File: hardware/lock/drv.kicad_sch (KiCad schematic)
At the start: 9 parts, among them J3 SOLENOID 12V, Q1 AO3400A

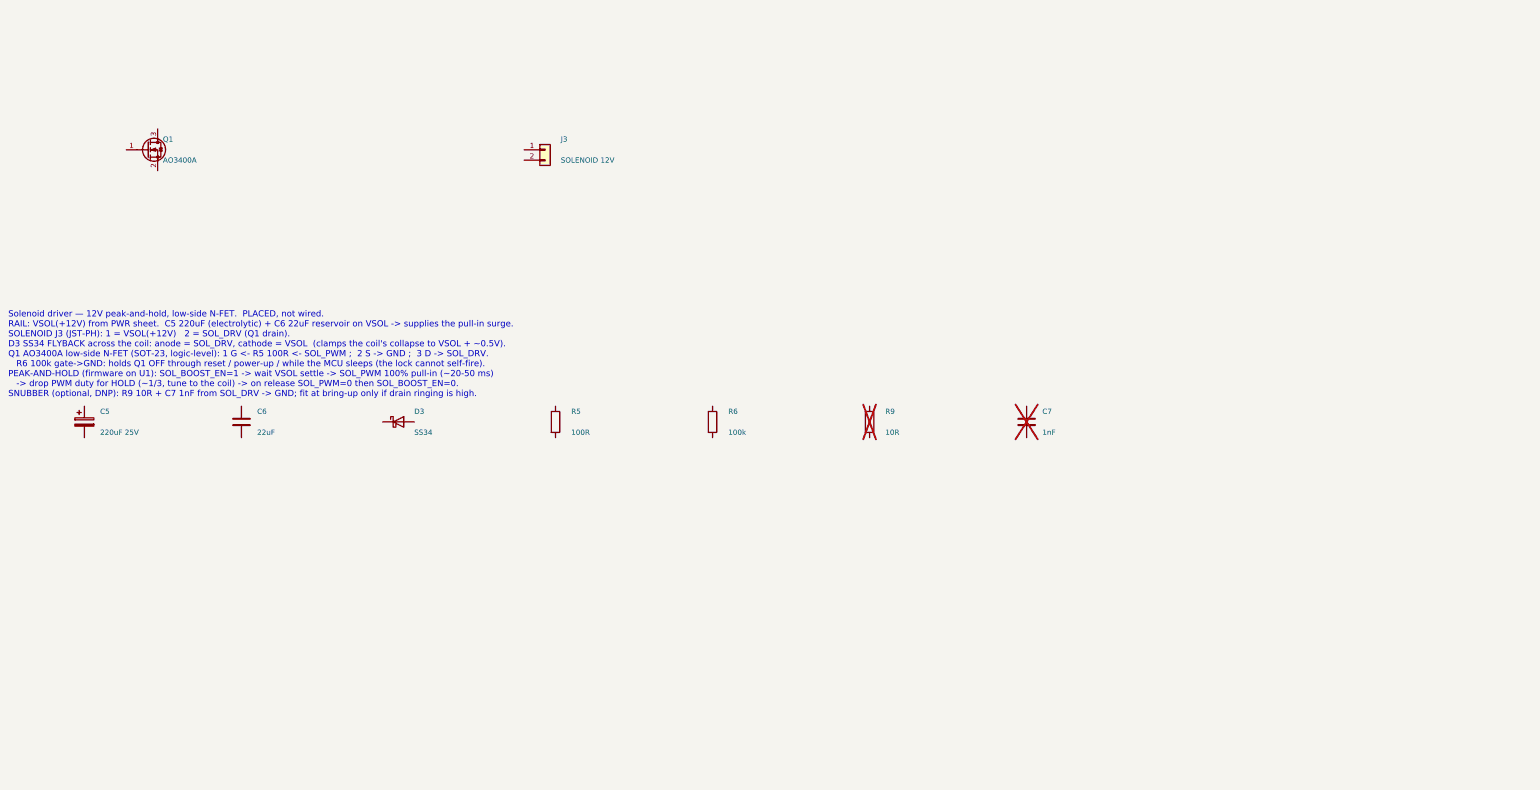
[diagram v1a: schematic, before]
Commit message: lock: servo option, firmware boost/power control, hall sensors, I2C protocol
Checkpoint of the companion lock board evolution:
- I2C link connector -> right-angle 4-pin JST-PH (S4B-PH-K, C157926);
  VCC is No-Connect on the lock (don't bridge the two battery rails).
- Add a parallel servo actuator option (J5) beside the 12V solenoid; one
  fully-populated board can carry both, one active at a time.
- Firmware-selectable boost: BOOST_VSEL (Q2 + R17 switch the FB divider)
  -> 6V (servo, default) or 12V (solenoid).  R4 22k / R17 20k.
- Servo high-side load switch (Q3 P-FET + Q4 driver, SERVO_PWR_EN) with a
  hardware interlock (Q5) that forces servo power OFF whenever boost = 12V,
  so a 12V solenoid pulse can never reach a 6V servo.
- Door/bolt hall sensors (J6/J7, S3B-PH-K) powered from a GPIO (HALL_PWR)
  so they draw ~0uA when the lock sleeps.
- I2C register/command protocol: STATUS (door/bolt/actuator probe, no auth),
  NONCE (read), COMMAND (authenticated UNLOCK/LOCK; LOCK drives a servo to the
  lock angle).  HMAC-SHA1 challenge-response, reuses smalltotp.

All footprints are KiCad-bundled (every part carries a 3D model). Board
regenerates + checks clean (46 components). Docs: hardware/lock/README.md and
DESIGN.md updated.

Co-Authored-By: Claude Opus 4.8 (1M context) <noreply@anthropic.com>
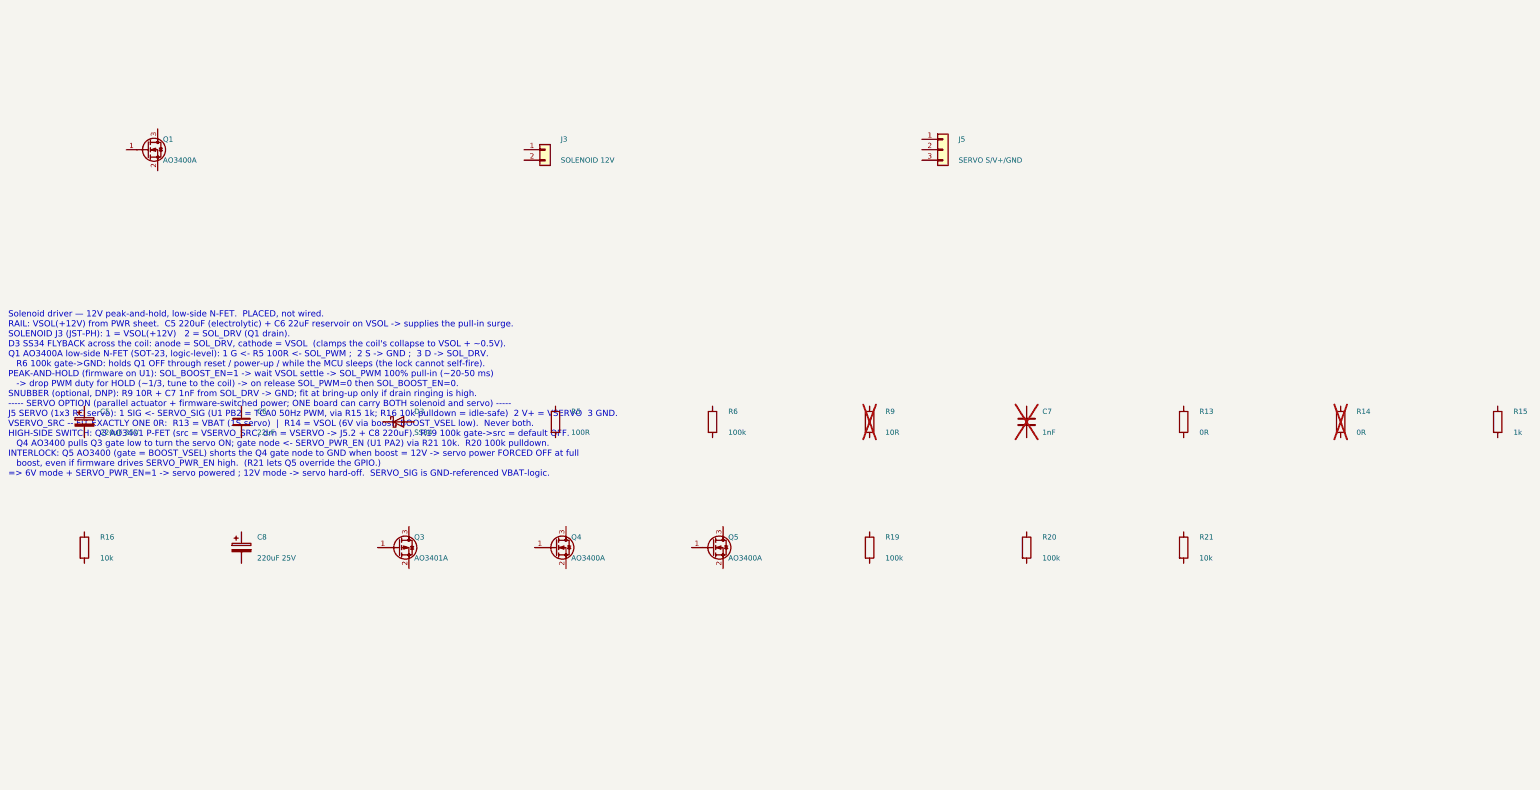
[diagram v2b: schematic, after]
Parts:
- added C8: 220uF 25V, Capacitor_SMD:CP_Elec_6.3x7.7, symbol Device:C_Polarized
- added J5: SERVO S/V+/GND, Connector_PinHeader_2.54mm:PinHeader_1x03_P2.54mm_Vertical, symbol Connector_Generic:Conn_01x03
- added Q3: AO3401A, Package_TO_SOT_SMD:SOT-23, symbol Transistor_FET:Q_PMOS_GSD
- added Q4, Q5: AO3400A, Package_TO_SOT_SMD:SOT-23, symbol Transistor_FET:Q_NMOS_GSD
- added R13, R14: 0R, Resistor_SMD:R_0402_1005Metric, symbol Device:R
- added R15: 1k, Resistor_SMD:R_0402_1005Metric, symbol Device:R
- added R16, R21: 10k, Resistor_SMD:R_0402_1005Metric, symbol Device:R
- added R19, R20: 100k, Resistor_SMD:R_0402_1005Metric, symbol Device:R
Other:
- title: lock — 12V solenoid driver (peak-and-hold) -> lock — Actuator: solenoid (12V peak-hold) OR servo (Vbat / 6V) -- build one

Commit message: lock: second servo output, clearer wiring notes, start PCB layout
- Add a second servo output (J8 + SERVO_SIG2 on PB4, R24/R25) sharing the
  VSERVO rail and the load-switch/interlock -- e.g. a dual-latch lock.
- Rewrite the per-sheet wiring notes (MCU/PWR/DRV) from prose into terse
  pin -> net maps: one line per part, every pin = its net, with a NETS IN
  header for cross-sheet signals. Rationale stays in the README.
- kschgen: park the wiring note below all placed components so the text no
  longer overlaps symbols (computed from the last component row).
- Start the lock PCB layout (hardware/lock/lock.kicad_pcb).

Board regenerates + checks clean (49 components; all footprints carry 3D models).

Co-Authored-By: Claude Opus 4.8 (1M context) <noreply@anthropic.com>
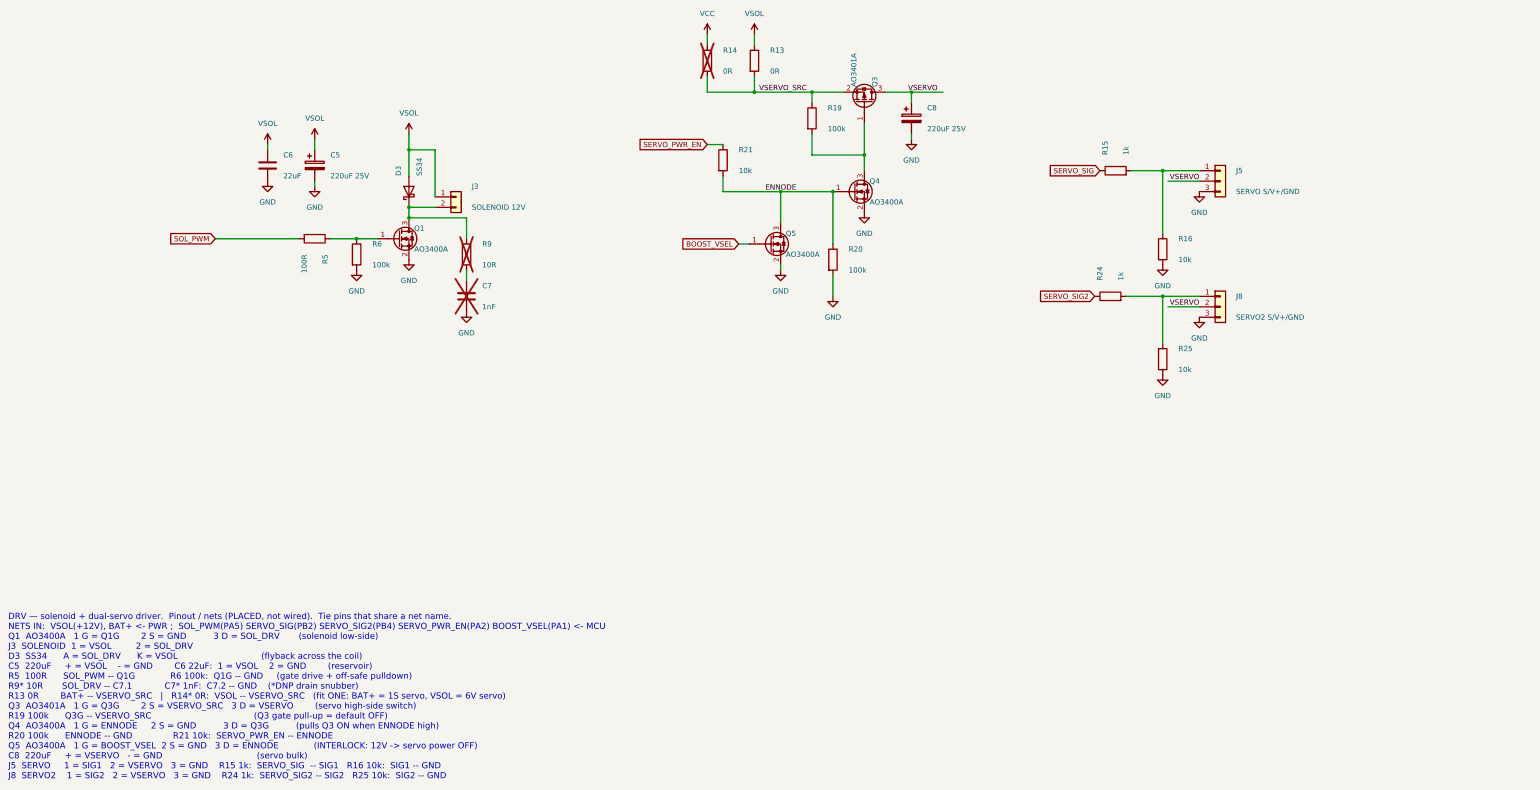
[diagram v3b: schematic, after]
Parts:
- added J8: SERVO2 S/V+/GND, Connector_PinHeader_2.54mm:PinHeader_1x03_P2.54mm_Vertical, symbol Connector_Generic:Conn_01x03
- added R24: 1k, Resistor_SMD:R_0402_1005Metric, symbol Device:R
- added R25: 10k, Resistor_SMD:R_0402_1005Metric, symbol Device:R
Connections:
- net SERVO_PWR_EN: now reaches R21.1
- net ENNODE: now reaches R21.2
- net ENNODE: now also Q4.1 (G), Q5.3 (D), R20.1
- net at Q1.1 (G): now also R5.1, R6.1
- net GND: now reaches Q1.2 (S)
- net GND: now also C5.2, C6.2, C7.2, C8.2, J5.3 (Pin_3), Q4.2 (S), Q5.2 (S), R16.2, R20.2, R6.2, J8.3 (Pin_3), R25.2
- net at Q1.3 (D): now also D3.1 (K), J3.2 (Pin_2), R9.1
- net VSOL: now reaches C5.1
- net VSOL: now also C6.1, D3.2 (A), J3.1 (Pin_1), R13.1
- net BOOST_VSEL: now reaches Q5.1 (G)
- net at R9.2: now also C7.1
- net VCC: now reaches R14.1
- net VSERVO_SRC: now reaches R14.2
- net VSERVO_SRC: now also Q3.2 (S), R13.2, R19.1
- net VSERVO: now reaches C8.1
- net VSERVO: now also J5.2 (Pin_2), Q3.3 (D), J8.2 (Pin_2)
- net at R19.2: now also Q3.1 (G), Q4.3 (D)
- net SOL_PWM: now reaches R5.2
- net at J5.1 (Pin_1): now also R15.2, R16.1
- net SERVO_SIG: now reaches R15.1
- new net: J8.1 (Pin_1), R24.2, R25.1
- new net SERVO_SIG2: R24.1
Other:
- note added: "DRV — solenoid + dual-servo driver. Pinout / nets (PLACED, not wired). Tie pins that share a net name. NETS IN: VSOL(+12V), BAT+ <- PWR ; SOL_PWM(PA5) SERVO_SIG(PB2) SERVO_SIG2(PB4) SERVO_PWR_EN(PA2) BOOST_VSEL(PA1) <- MCU Q1 AO3400A 1 G = Q1G 2 S = GND 3 D = SOL_DRV (solenoid low-side) J3 SOLENOID 1 = VSOL 2 = SOL_DRV D3 SS34 A = SOL_DRV K = VSOL (flyback across the coil) C5 220uF + = VSOL - = G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"
- note removed: "Solenoid driver — 12V peak-and-hold, low-side N-FET. PLACED, not wired. RAIL: VSOL(+12V) from PWR sheet. C5 220uF (electrolytic) + C6 22uF reservoir on VSOL -> supplies the pull-in surge. SOLENOID J3 (JST-PH): 1 = VSOL(+12V) 2 = SOL_DRV (Q1 drain). D3 SS34 FLYBACK across the coil: anode = SOL_DRV, cathode = VSOL (clamps the coil's collapse to VSOL + ~0.5V). Q1 AO3400A low-side N-FET (SOT-23, logi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"

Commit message: lock: 220uF 25V C5/C8 -> C4747974 (RST220UF25V019), Economic-eligible
Swap the reservoir/servo-bulk electrolytic from C2918361 (not available for
JLCPCB Economic assembly) to C4747974 — same D6.3xL7.7mm body, Economic-eligible.
Updated schematic (C5/C8), manifest, README BOM, and BUILD.md; remade BOM/CPL
(BOM<->CPL still match exactly, 42=42).

Co-Authored-By: Claude Opus 4.8 (1M context) <noreply@anthropic.com>
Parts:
- C5, C8: LCSC C2918361 -> C4747974; MPN RVT1E221M0607 -> RST220UF25V019; Manufacturer Rubycon-alt -> generic
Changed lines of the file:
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@@
 			)
 		)
-		(property "LCSC" "C2918361"
+		(property "LCSC" "C4747974"
 			(at 86.36 59.69 0)
 			(hide yes)
@@
 			)
 		)
-		(property "MPN" "RVT1E221M0607"
+		(property "MPN" "RST220UF25V019"
 			(at 86.36 59.69 0)
 			(hide yes)
@@
 			)
 		)
-		(property "Manufacturer" "Rubycon-alt"
+		(property "Manufacturer" "generic"
 			(at 86.36 59.69 0)
 			(hide yes)
@@
 			)
 		)
-		(property "LCSC" "C2918361"
+		(property "LCSC" "C4747974"
 			(at 231.14 48.26 0)
 			(hide yes)
@@
 			)
 		)
-		(property "MPN" "RVT1E221M0607"
+		(property "MPN" "RST220UF25V019"
 			(at 231.14 48.26 0)
 			(hide yes)
@@
 			)
 		)
-		(property "Manufacturer" "Rubycon-alt"
+		(property "Manufacturer" "generic"
 			(at 231.14 48.26 0)
 			(hide yes)

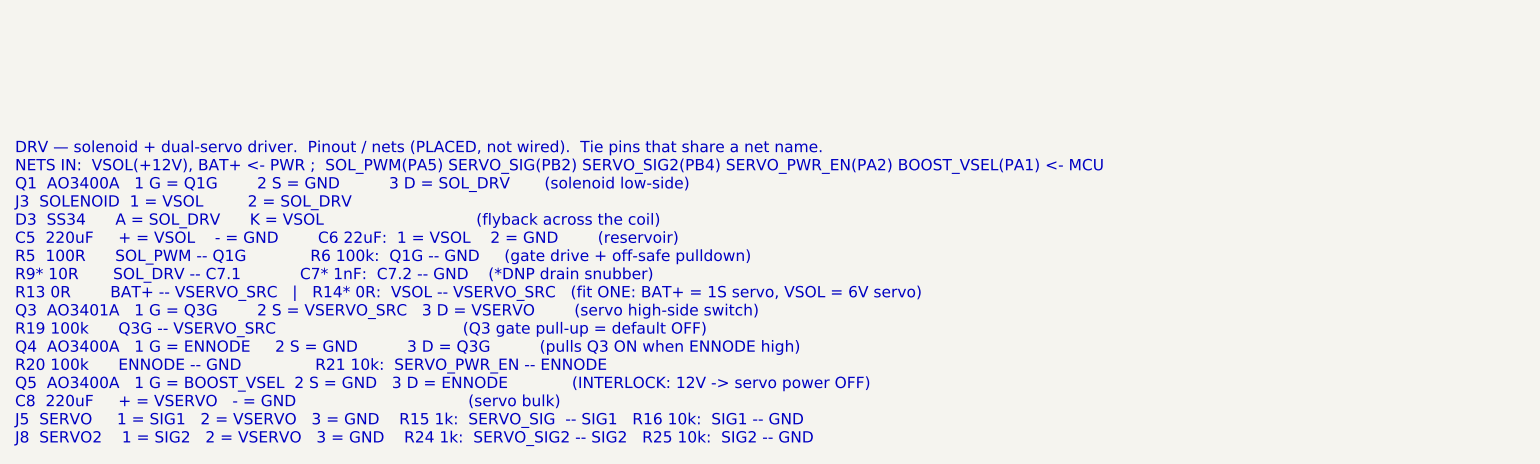
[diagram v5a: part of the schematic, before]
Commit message: hardware: fix PSU load-share S/D, make all sheet notes monospace
The PSU wiring note specified Q1 (AO3401A load-share PMOS) as S=BAT+,
D=VSYS. A PMOS body diode conducts D->S, so that orientation points the
diode VSYS -> BAT+: with USB attached VSYS sits ~4.7V (VBUS - D3) against
a 3.0-4.2V cell, forward-biasing it and dumping uncontrolled current into
the battery, bypassing the MCP73831 charger entirely.

Correct assignment is D=BAT+, S=VSYS, so the body diode points BAT+ ->
VSYS: the battery always reaches the load, and USB can never back-feed
the cell. Q1 was placed but never wired (all three pins are unconnected
in the netlist), so this is a spec fix ahead of wiring, not a board
change. The lock's Q3 is a high-side switch and deliberately uses the
opposite S/D assignment; the note now says so, to stop the two being
"reconciled" by pattern-matching.

Also relaid the PSU note as a two-column table and gave every sheet note
the Courier New face the generator already emits (kschgen NOTE_FONT, added
in 43a6067). The sheets predate that commit, so their notes rendered in
KiCad's variable-width stroke font and the space-padded pin tables did not
line up. Font only on the other six notes -- text is untouched.

Verified: kicad-cli netlists for both boards are byte-identical before and
after (ephemerkey 259 nodes, lock 131 nodes) once the export timestamp is
excluded; no non-font lines changed in any sheet; all sheets re-rendered
and the notes fit inside the page frame.

The four ephemerkey sheets also carry pre-existing eeschema reformatting
(expanded lib_symbols) that was already in the working tree.

Co-Authored-By: Claude Opus 4.8 (1M context) <noreply@anthropic.com>
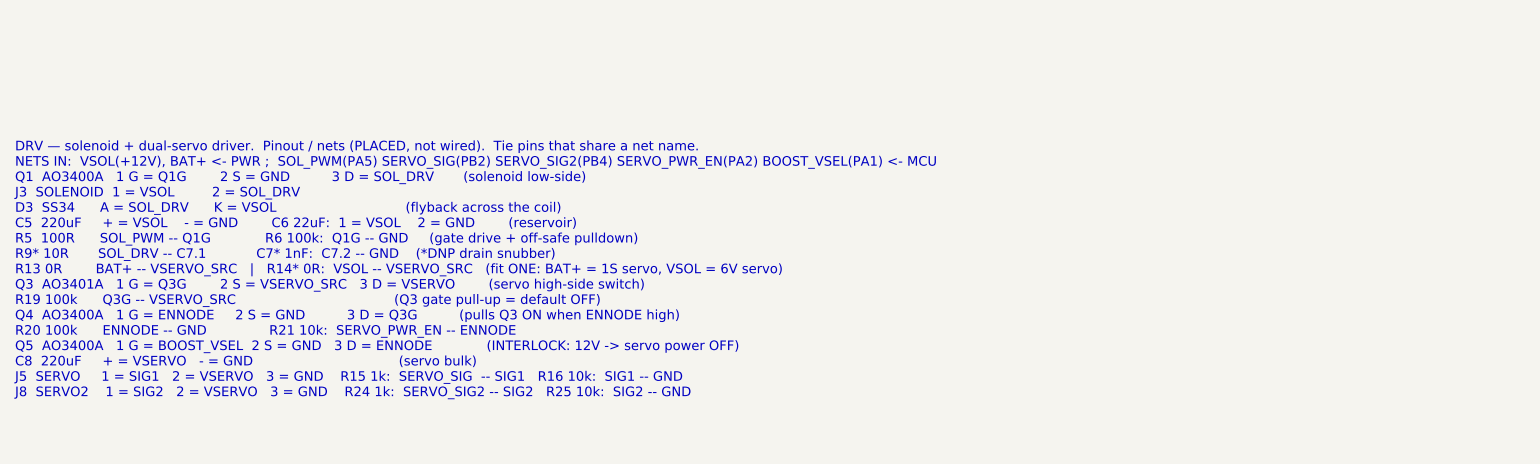
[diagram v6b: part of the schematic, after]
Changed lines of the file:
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@@
 		(effects
 			(font
-				(size 1.5 1.5)
+				(face "Courier New")
+				(size 1.27 1.27)
 			)
 			(justify left top)
